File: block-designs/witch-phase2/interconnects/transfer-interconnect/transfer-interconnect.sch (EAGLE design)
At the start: 14 parts

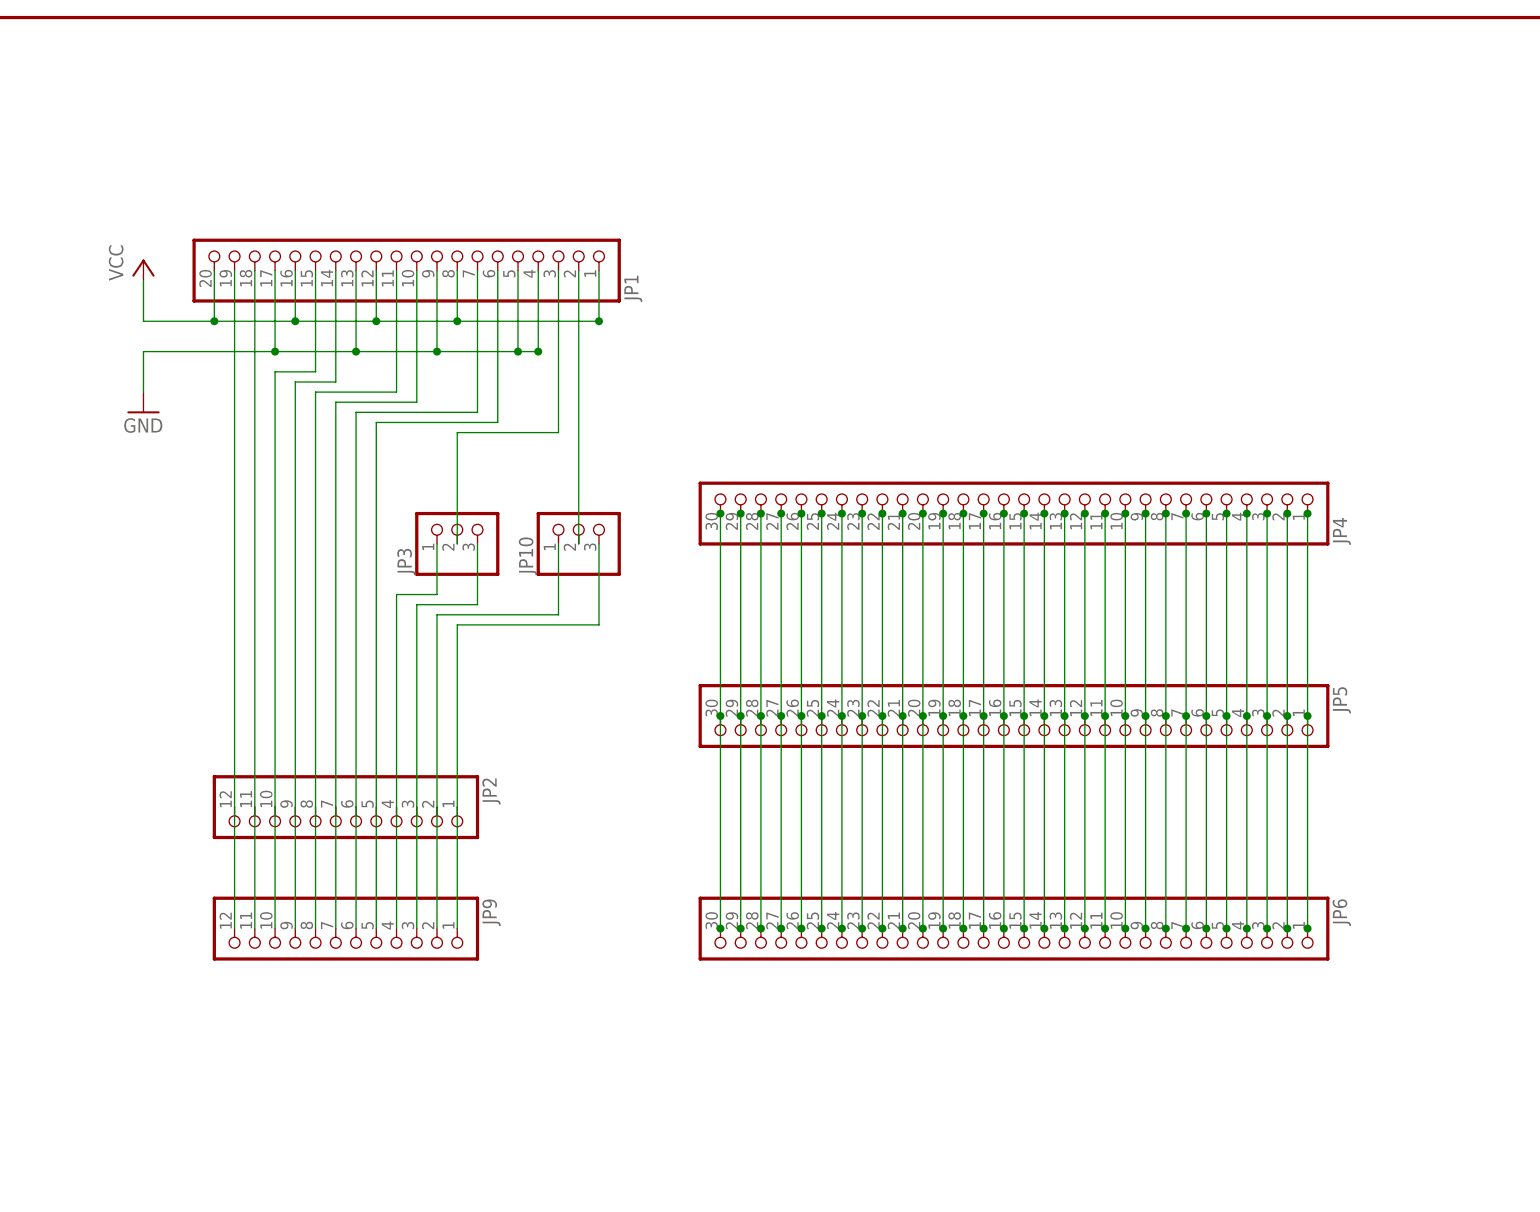
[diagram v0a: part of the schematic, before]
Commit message: fixes for layout and connections
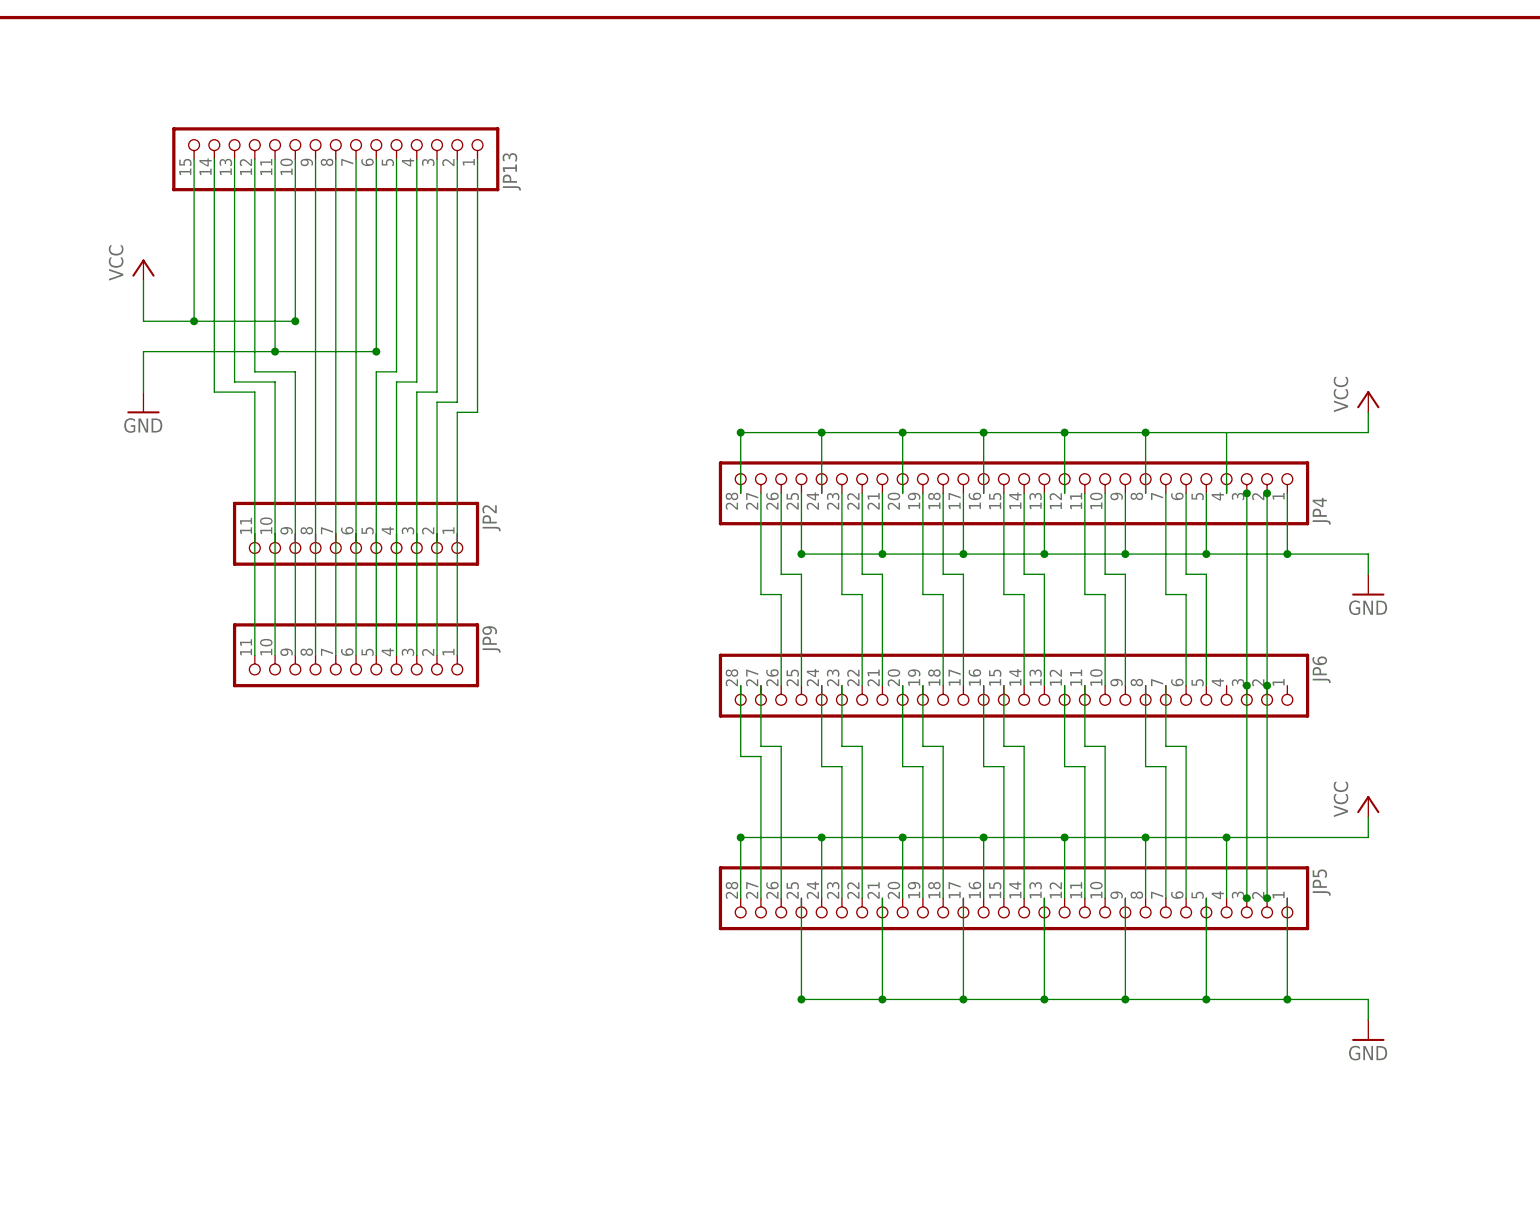
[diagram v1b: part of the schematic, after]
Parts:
- removed JP1: (no value), pinhead:PINHD-1X20
- removed JP10, JP3: (no value), pinhead:PINHD-1X3
- added JP13: (no value), pinhead:PINHD-1X15
- JP2, JP9: device pinhead:PINHD-1X12 -> pinhead:PINHD-1X11
- JP4, JP5, JP6: device pinhead:PINHD-1X30 -> pinhead:PINHD-1X28
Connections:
- removed net N$1 (its old number): JP4.30, JP5.30, JP6.30
- removed net N$2 (its old number): JP4.29, JP5.29, JP6.29
- removed net N$27: JP4.4, JP5.4, JP6.4
- removed net N$30: JP4.1, JP5.1, JP6.1
- removed net N$31: JP1.19, JP2.12, JP9.12
- removed net N$43: JP1.3, JP3.2
- removed net N$44: JP1.2, JP10.2
- net GND: now also JP13.11, JP13.6, JP4.1, JP4.13, JP4.17, JP4.21, JP4.25, JP4.5, JP4.9, JP5.1, JP5.13, JP5.17, JP5.21, JP5.25, JP5.5, JP5.9; no longer JP1.13, JP1.17, JP1.4, JP1.5, JP1.9
- net N$10: now also JP4.19, JP6.18; no longer JP4.21, JP5.21, JP6.21
- net N$11: now also JP4.22, JP6.21; no longer JP4.20, JP5.20, JP6.20
- net N$12: now also JP4.23, JP6.22; no longer JP4.19, JP5.19, JP6.19
- net N$13: now also JP4.26, JP6.25; no longer JP4.18, JP5.18, JP6.18
- net N$14: now also JP4.27, JP6.26; no longer JP4.17, JP5.17, JP6.17
- net N$15: now also JP5.6, JP6.7; no longer JP4.16, JP5.16, JP6.16
- net N$16: now also JP5.7, JP6.8; no longer JP4.15, JP5.15, JP6.15
- net N$17: now also JP5.10, JP6.11; no longer JP4.14, JP5.14, JP6.14
- net N$18: now also JP5.11, JP6.12; no longer JP4.13, JP5.13, JP6.13
- net N$19: now also JP5.14, JP6.15; no longer JP4.12, JP5.12, JP6.12
- net N$20: now also JP5.15, JP6.16; no longer JP4.11, JP5.11, JP6.11
- net N$21: now also JP5.18, JP6.19; no longer JP4.10, JP5.10, JP6.10
- net N$22: now also JP5.19, JP6.20; no longer JP4.9, JP5.9, JP6.9
- net N$23: now also JP5.22, JP6.23; no longer JP4.8, JP5.8, JP6.8
- net N$24: now also JP5.23, JP6.24; no longer JP4.7, JP5.7, JP6.7
- net N$25: now also JP5.26, JP6.27; no longer JP4.6, JP5.6, JP6.6
- net N$26: now also JP5.27, JP6.28; no longer JP4.5, JP5.5, JP6.5
- net N$3: now also JP4.10, JP6.9; no longer JP4.28, JP5.28, JP6.28
- net N$32: now also JP13.14; no longer JP1.18
- net N$33: now also JP13.13; no longer JP1.15
- net N$34: now also JP13.12; no longer JP1.14
- net N$35: now also JP13.9; no longer JP1.11
- net N$36: now also JP13.8; no longer JP1.10
- net N$37: now also JP13.7; no longer JP1.7
- net N$38: now also JP13.5; no longer JP1.6
- net N$39: now also JP13.4; no longer JP3.1
- net N$4: now also JP4.11, JP6.10; no longer JP4.27, JP5.27, JP6.27
- net N$40: now also JP13.3; no longer JP3.3
- net N$41: now also JP13.2; no longer JP10.1
- net N$46: now also JP13.1; no longer JP10.3
- net N$5: now also JP4.6, JP6.5; no longer JP4.26, JP5.26, JP6.26
- net N$6: now also JP4.7, JP6.6; no longer JP4.25, JP5.25, JP6.25
- net N$7: now also JP4.14, JP6.13; no longer JP4.24, JP5.24, JP6.24
- net N$8: now also JP4.15, JP6.14; no longer JP4.23, JP5.23, JP6.23
- net N$9: now also JP4.18, JP6.17; no longer JP4.22, JP5.22, JP6.22
- net VCC: now also JP13.10, JP13.15, JP4.12, JP4.16, JP4.20, JP4.24, JP4.28, JP4.4, JP4.8, JP5.12, JP5.16, JP5.20, JP5.24, JP5.28, JP5.4, JP5.8; no longer JP1.1, JP1.12, JP1.16, JP1.20, JP1.8

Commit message: add schmitt-triggers to receive signals
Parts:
- added C10, C11, C12, C13, C14, C15, C16, C17, C18, C19, C20, C21, C22, C23, C24, C25, C26, C3, C4, C5, C6, C7, C8, C9: 1uF, resistor:C-USC0603K
- added IC1, IC10, IC11, IC12, IC2, IC3, IC4, IC5, IC6, IC7, IC8, IC9: 74LVC1G14DBV, 74xx-little-us:74LVC1G14DBV
- added R1, R10, R11, R12, R2, R3, R4, R5, R6, R7, R8, R9: 100k, resistor:R-US_R0603
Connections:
- removed net N$10: JP4.19, JP6.18
- removed net N$12: JP4.23, JP6.22
- removed net N$14: JP4.27, JP6.26
- removed net N$16: JP5.7, JP6.8
- removed net N$18: JP5.11, JP6.12
- removed net N$20: JP5.15, JP6.16
- removed net N$22: JP5.19, JP6.20
- removed net N$24: JP5.23, JP6.24
- removed net N$26: JP5.27, JP6.28
- removed net N$4: JP4.11, JP6.10
- removed net N$6: JP4.7, JP6.6
- removed net N$8: JP4.15, JP6.14
- new net IN5: C8.1, IC6A.I, R6.1
- new net IN6: C9.1, IC7A.I, R7.1
- new net INA1: C4.1, IC1A.I, JP6.26, R1.1
- new net INA2: C5.1, IC3A.I, JP6.22, R3.1
- new net INA3: C6.1, IC4A.I, JP6.18, R4.1
- new net INA4: C7.1, IC5A.I, JP6.14, R5.1
- new net INA5: JP6.10
- new net INA6: JP6.6
- new net INB1: C3.1, IC2A.I, JP6.28, R2.1
- new net INB2: C10.1, IC8A.I, JP6.24, R8.1
- new net INB3: C11.1, IC9A.I, JP6.20, R9.1
- new net INB4: C12.1, IC10A.I, JP6.16, R10.1
- new net INB5: C13.1, IC11A.I, JP6.12, R11.1
- new net INB6: C14.1, IC12A.I, JP6.8, R12.1
- new net OUTA1: IC1A.O, JP4.27
- new net OUTA2: IC3A.O, JP4.23
- new net OUTA3: IC4A.O, JP4.19
- new net OUTA4: IC5A.O, JP4.15
- new net OUTA5: IC6A.O, JP4.11
- new net OUTA6: IC7A.O, JP4.7
- new net OUTB1: IC2A.O, JP5.27
- new net OUTB2: IC8A.O, JP5.23
- new net OUTB3: IC9A.O, JP5.19
- new net OUTB4: IC10A.O, JP5.15
- new net OUTB5: IC11A.O, JP5.11
- new net OUTB6: IC12A.O, JP5.7
- net GND: now also C10.2, C11.2, C12.2, C13.2, C14.2, C15.2, C16.2, C17.2, C18.2, C19.2, C20.2, C21.2, C22.2, C23.2, C24.2, C25.2, C26.2, C3.2, C4.2, C5.2, C6.2, C7.2, C8.2, C9.2
- net VCC: now also C15.1, C16.1, C17.1, C18.1, C19.1, C20.1, C21.1, C22.1, C23.1, C24.1, C25.1, C26.1, R1.2, R10.2, R11.2, R12.2, R2.2, R3.2, R4.2, R5.2, R6.2, R7.2, R8.2, R9.2

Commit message: minor cleanup
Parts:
- IC1, IC10, IC11, IC12, IC2, IC3, IC4, IC5, IC6, IC7, IC8, IC9: value 74LVC1G14DBV -> 74LVC1G17DBV; device 74xx-little-us:74LVC1G14DBV -> 74xx-little-us:74LVC1G17DBV
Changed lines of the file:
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@@
 <part name="P+7" library="supply1" deviceset="VCC" device=""/>
 <part name="R1" library="resistor" deviceset="R-US_" device="R0603" value="100k"/>
-<part name="IC1" library="74xx-little-us" deviceset="74*1G14" device="DBV" technology="LVC"/>
+<part name="IC1" library="74xx-little-us" deviceset="74*1G17" device="DBV" technology="LVC"/>
 <part name="FRAME2" library="frames" deviceset="TABL_L" device=""/>
 <part name="C5" library="resistor" deviceset="C-US" device="C0603K" value="1uF"/>
@@
 <part name="P+8" library="supply1" deviceset="VCC" device=""/>
 <part name="R3" library="resistor" deviceset="R-US_" device="R0603" value="100k"/>
-<part name="IC3" library="74xx-little-us" deviceset="74*1G14" device="DBV" technology="LVC"/>
+<part name="IC3" library="74xx-little-us" deviceset="74*1G17" device="DBV" technology="LVC"/>
 <part name="C6" library="resistor" deviceset="C-US" device="C0603K" value="1uF"/>
 <part name="GND9" library="supply1" deviceset="GND" device=""/>
 <part name="P+9" library="supply1" deviceset="VCC" device=""/>
 <part name="R4" library="resistor" deviceset="R-US_" device="R0603" value="100k"/>
-<part name="IC4" library="74xx-little-us" deviceset="74*1G14" device="DBV" technology="LVC"/>
+<part name="IC4" library="74xx-little-us" deviceset="74*1G17" device="DBV" technology="LVC"/>
 <part name="C7" library="resistor" deviceset="C-US" device="C0603K" value="1uF"/>
 <part name="GND10" library="supply1" deviceset="GND" device=""/>
 <part name="P+10" library="supply1" deviceset="VCC" device=""/>
 <part name="R5" library="resistor" deviceset="R-US_" device="R0603" value="100k"/>
-<part name="IC5" library="74xx-little-us" deviceset="74*1G14" device="DBV" technology="LVC"/>
+<part name="IC5" library="74xx-little-us" deviceset="74*1G17" device="DBV" technology="LVC"/>
 <part name="C8" library="resistor" deviceset="C-US" device="C0603K" value="1uF"/>
 <part name="GND11" library="supply1" deviceset="GND" device=""/>
 <part name="P+11" library="supply1" deviceset="VCC" device=""/>
 <part name="R6" library="resistor" deviceset="R-US_" device="R0603" value="100k"/>
-<part name="IC6" library="74xx-little-us" deviceset="74*1G14" device="DBV" technology="LVC"/>
+<part name="IC6" library="74xx-little-us" deviceset="74*1G17" device="DBV" technology="LVC"/>
 <part name="C9" library="resistor" deviceset="C-US" device="C0603K" value="1uF"/>
 <part name="GND12" library="supply1" deviceset="GND" device=""/>
 <part name="P+12" library="supply1" deviceset="VCC" device=""/>
 <part name="R7" library="resistor" deviceset="R-US_" device="R0603" value="100k"/>
-<part name="IC7" library="74xx-little-us" deviceset="74*1G14" device="DBV" technology="LVC"/>
+<part name="IC7" library="74xx-little-us" deviceset="74*1G17" device="DBV" technology="LVC"/>
 <part name="FRAME3" library="frames" deviceset="TABL_L" device=""/>
 <part name="C3" library="resistor" deviceset="C-US" device="C0603K" value="1uF"/>
@@
 <part name="P+6" library="supply1" deviceset="VCC" device=""/>
 <part name="R2" library="resistor" deviceset="R-US_" device="R0603" value="100k"/>
-<part name="IC2" library="74xx-little-us" deviceset="74*1G14" device="DBV" technology="LVC"/>
+<part name="IC2" library="74xx-little-us" deviceset="74*1G17" device="DBV" technology="LVC"/>
 <part name="C10" library="resistor" deviceset="C-US" device="C0603K" value="1uF"/>
 <part name="GND13" library="supply1" deviceset="GND" device=""/>
 <part name="P+13" library="supply1" deviceset="VCC" device=""/>
 <part name="R8" library="resistor" deviceset="R-US_" device="R0603" value="100k"/>
-<part name="IC8" library="74xx-little-us" deviceset="74*1G14" device="DBV" technology="LVC"/>
+<part name="IC8" library="74xx-little-us" deviceset="74*1G17" device="DBV" technology="LVC"/>
 <part name="C11" library="resistor" deviceset="C-US" device="C0603K" value="1uF"/>
 <part name="GND14" library="supply1" deviceset="GND" device=""/>
 <part name="P+14" library="supply1" deviceset="VCC" device=""/>
 <part name="R9" library="resistor" deviceset="R-US_" device="R0603" value="100k"/>
-<part name="IC9" library="74xx-little-us" deviceset="74*1G14" device="DBV" technology="LVC"/>
+<part name="IC9" library="74xx-little-us" deviceset="74*1G17" device="DBV" technology="LVC"/>
 <part name="C12" library="resistor" deviceset="C-US" device="C0603K" value="1uF"/>
 <part name="GND15" library="supply1" deviceset="GND" device=""/>
 <part name="P+15" library="supply1" deviceset="VCC" device=""/>
 <part name="R10" library="resistor" deviceset="R-US_" device="R0603" value="100k"/>
-<part name="IC10" library="74xx-little-us" deviceset="74*1G14" device="DBV" technology="LVC"/>
+<part name="IC10" library="74xx-little-us" deviceset="74*1G17" device="DBV" technology="LVC"/>
 <part name="C13" library="resistor" deviceset="C-US" device="C0603K" value="1uF"/>
 <part name="GND16" library="supply1" deviceset="GND" device=""/>
 <part name="P+16" library="supply1" deviceset="VCC" device=""/>
 <part name="R11" library="resistor" deviceset="R-US_" device="R0603" value="100k"/>
-<part name="IC11" library="74xx-little-us" deviceset="74*1G14" device="DBV" technology="LVC"/>
+<part name="IC11" library="74xx-little-us" deviceset="74*1G17" device="DBV" technology="LVC"/>
 <part name="C14" library="resistor" deviceset="C-US" device="C0603K" value="1uF"/>
 <part name="GND17" library="supply1" deviceset="GND" device=""/>
 <part name="P+17" library="supply1" deviceset="VCC" device=""/>
 <part name="R12" library="resistor" deviceset="R-US_" device="R0603" value="100k"/>
-<part name="IC12" library="74xx-little-us" deviceset="74*1G14" device="DBV" technology="LVC"/>
+<part name="IC12" library="74xx-little-us" deviceset="74*1G17" device="DBV" technology="LVC"/>
 <part name="C15" library="resistor" deviceset="C-US" device="C0603K" value="1uF"/>
 <part name="GND18" library="supply1" deviceset="GND" device=""/>
